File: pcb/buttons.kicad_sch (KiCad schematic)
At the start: 13 parts, among them SW1 SW_MEC_5E, SW10 SW_MEC_5E, SW11 SW_MEC_5E, SW12 SW_MEC_5E, SW13 SW_DIP_x06, SW2 SW_MEC_5E, SW3 SW_MEC_5E, SW4 SW_MEC_5E, SW5 SW_MEC_5E, SW6 SW_MEC_5E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

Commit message: Fixed ERC and DRC
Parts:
- SW1, SW10, SW11, SW12, SW2, SW3, SW4, SW5, SW6, SW7, SW8, SW9: LCSC (none) -> C318884
- SW13: LCSC (none) -> C54952
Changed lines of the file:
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@@
+      (effects (font (size 1.27 1.27)) hide)
+    )
+    (property "LCSC" "C318884" (id 4) (at 207.01 76.2 0)
       (effects (font (size 1.27 1.27)) hide)
     )
@@
       (effects (font (size 1.27 1.27)) hide)
     )
+    (property "LCSC" "C318884" (id 4) (at 181.61 95.25 0)
+      (effects (font (size 1.27 1.27)) hide)
+    )
     (pin "1")
     (pin "2")
@@
       (effects (font (size 1.27 1.27)) hide)
     )
+    (property "LCSC" "C318884" (id 4) (at 181.61 76.2 0)
+      (effects (font (size 1.27 1.27)) hide)
+    )
     (pin "1")
     (pin "2")
@@
       (effects (font (size 1.27 1.27)) hide)
     )
+    (property "LCSC" "C318884" (id 4) (at 157.48 76.2 0)
+      (effects (font (size 1.27 1.27)) hide)
+    )
     (pin "1")
     (pin "2")
@@
       (effects (font (size 1.27 1.27)) hide)
     )
+    (property "LCSC" "C318884" (id 4) (at 157.48 95.25 0)
+      (effects (font (size 1.27 1.27)) hide)
+    )
     (pin "1")
     (pin "2")
@@
       (effects (font (size 1.27 1.27)) hide)
     )
+    (property "LCSC" "C318884" (id 4) (at 134.62 95.25 0)
+      (effects (font (size 1.27 1.27)) hide)
+    )
     (pin "1")
     (pin "2")
@@
       (effects (font (size 1.27 1.27)) hide)
     )
+    (property "LCSC" "C318884" (id 4) (at 207.01 95.25 0)
+      (effects (font (size 1.27 1.27)) hide)
+    )
     (pin "1")
     (pin "2")
@@
       (effects (font (size 1.27 1.27)) hide)
     )
+    (property "LCSC" "C318884" (id 4) (at 113.03 95.25 0)
+      (effects (font (size 1.27 1.27)) hide)
+    )
     (pin "1")
     (pin "2")
@@
     )
     (property "Datasheet" "~" (id 3) (at 165.1 129.54 0)
+      (effects (font (size 1.27 1.27)) hide)
+    )
+    (property "LCSC" "C54952" (id 4) (at 165.1 129.54 0)
       (effects (font (size 1.27 1.27)) hide)
     )
@@
       (effects (font (size 1.27 1.27)) hide)
     )
+    (property "LCSC" "C318884" (id 4) (at 231.14 95.25 0)
+      (effects (font (size 1.27 1.27)) hide)
+    )
     (pin "1")
     (pin "2")
@@
       (effects (font (size 1.27 1.27)) hide)
     )
+    (property "LCSC" "C318884" (id 4) (at 134.62 76.2 0)
+      (effects (font (size 1.27 1.27)) hide)
+    )
     (pin "1")
     (pin "2")
@@
       (effects (font (size 1.27 1.27)) hide)
     )
+    (property "LCSC" "C318884" (id 4) (at 231.14 76.2 0)
+      (effects (font (size 1.27 1.27)) hide)
+    )
     (pin "1")
     (pin "2")
@@
       (effects (font (size 1.27 1.27)) hide)
     )
+    (property "LCSC" "C318884" (id 4) (at 113.03 76.2 0)
+      (effects (font (size 1.27 1.27)) hide)
+    )

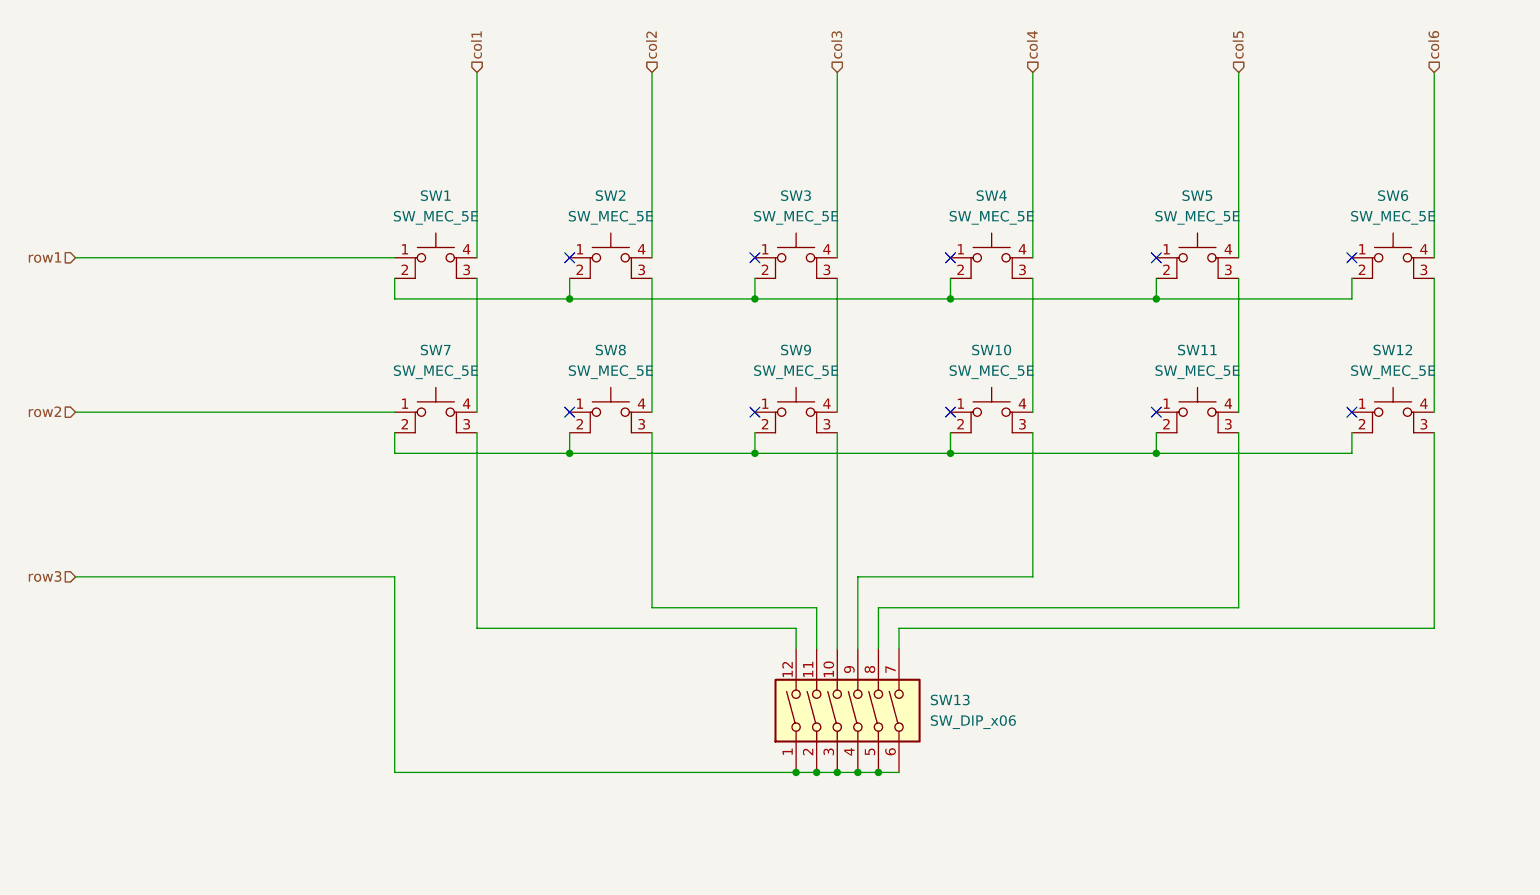
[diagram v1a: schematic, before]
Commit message: Added diodes to key matrix
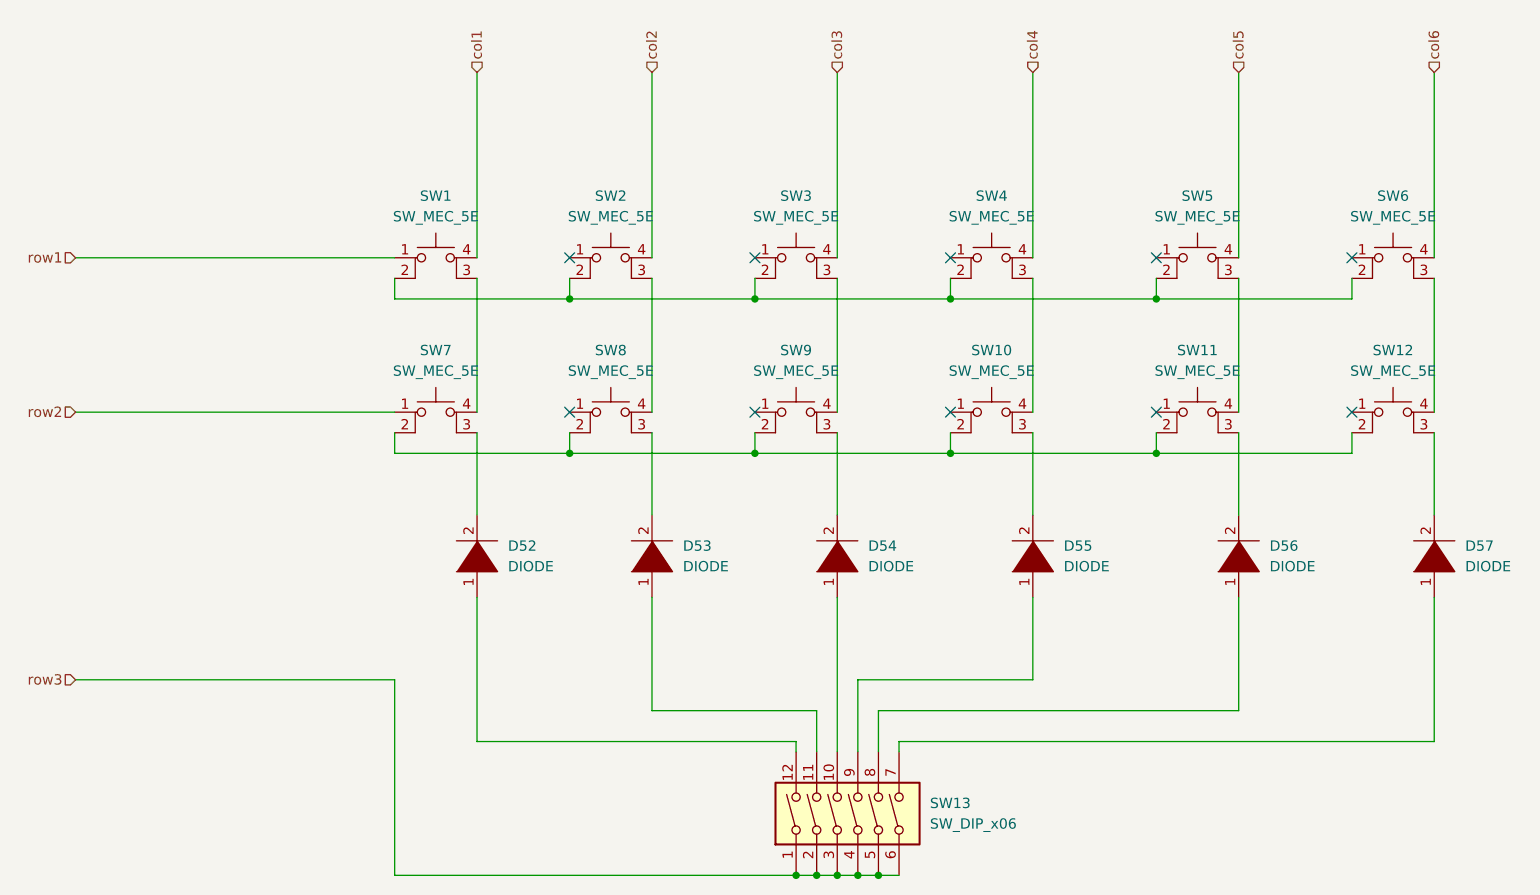
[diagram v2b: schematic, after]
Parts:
- added D52, D53, D54, D55, D56, D57: DIODE, Diode_SMD:D_SOD-123F, symbol pspice:DIODE
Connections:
- net at SW10.3 (K): now also D55.2 (A); no longer SW13.9
- net at SW9.3 (K): now also D54.2 (A); no longer SW13.10
- net at SW8.3 (K): now also D53.2 (A); no longer SW13.11
- net at SW11.3 (K): now also D56.2 (A); no longer SW13.8
- net at SW7.3 (K): now also D52.2 (A); no longer SW13.12
- net at SW13.7: now also D57.1 (K); no longer SW12.3 (K)
- new net: D57.2 (A), SW12.3 (K)
- new net: D56.1 (K), SW13.8
- new net: D54.1 (K), SW13.10
- new net: D53.1 (K), SW13.11
- new net: D52.1 (K), SW13.12
- new net: D55.1 (K), SW13.9
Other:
- moved on the sheet: SW13

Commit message: Small fixed for new board
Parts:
- D52, D53, D54, D55, D56, D57: symbol pspice:DIODE -> Diode:SM4007
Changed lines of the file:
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@@
-    (stroke (width 0) (type default) (color 0 0 0 0))
-  )
-  (wire (pts (xy 118.11 95.25) (xy 118.11 105.41))
     (stroke (width 0) (type default) (color 0 0 0 0))
   )
@@
     (stroke (width 0) (type default) (color 0 0 0 0))
   )
-  (wire (pts (xy 162.56 115.57) (xy 162.56 134.62))
+  (wire (pts (xy 162.56 114.3) (xy 162.56 134.62))
     (stroke (width 0) (type default) (color 0 0 0 0))
   )
@@
     (stroke (width 0) (type default) (color 0 0 0 0))
   )
-  (wire (pts (xy 186.69 95.25) (xy 186.69 105.41))
+  (wire (pts (xy 186.69 95.25) (xy 186.69 106.68))
     (stroke (width 0) (type default) (color 0 0 0 0))
   )
@@
     (stroke (width 0) (type default) (color 0 0 0 0))
   )
+  (wire (pts (xy 212.09 114.3) (xy 212.09 129.54))
+    (stroke (width 0) (type default) (color 0 0 0 0))
+  )
   (wire (pts (xy 139.7 76.2) (xy 139.7 92.71))
     (stroke (width 0) (type default) (color 0 0 0 0))
@@
     (stroke (width 0) (type default) (color 0 0 0 0))
   )
+  (wire (pts (xy 118.11 114.3) (xy 118.11 133.35))
+    (stroke (width 0) (type default) (color 0 0 0 0))
+  )
   (wire (pts (xy 167.64 134.62) (xy 167.64 129.54))
     (stroke (width 0) (type default) (color 0 0 0 0))
@@
     (stroke (width 0) (type default) (color 0 0 0 0))
   )
+  (wire (pts (xy 118.11 95.25) (xy 118.11 106.68))
+    (stroke (width 0) (type default) (color 0 0 0 0))
+  )
   (wire (pts (xy 201.93 95.25) (xy 201.93 97.79))
     (stroke (width 0) (type default) (color 0 0 0 0))
   )
-  (wire (pts (xy 212.09 95.25) (xy 212.09 105.41))
-    (stroke (width 0) (type default) (color 0 0 0 0))
-  )
-  (wire (pts (xy 139.7 115.57) (xy 139.7 129.54))
+  (wire (pts (xy 212.09 95.25) (xy 212.09 106.68))
     (stroke (width 0) (type default) (color 0 0 0 0))
   )
@@
     (stroke (width 0) (type default) (color 0 0 0 0))
   )
-  (wire (pts (xy 236.22 95.25) (xy 236.22 105.41))
+  (wire (pts (xy 236.22 95.25) (xy 236.22 106.68))
     (stroke (width 0) (type default) (color 0 0 0 0))
   )
@@
     (stroke (width 0) (type default) (color 0 0 0 0))
   )
-  (wire (pts (xy 162.56 95.25) (xy 162.56 105.41))
+  (wire (pts (xy 162.56 95.25) (xy 162.56 106.68))
     (stroke (width 0) (type default) (color 0 0 0 0))
   )
@@
     (stroke (width 0) (type default) (color 0 0 0 0))
   )
-  (wire (pts (xy 186.69 115.57) (xy 186.69 125.73))
+  (wire (pts (xy 186.69 114.3) (xy 186.69 125.73))
     (stroke (width 0) (type default) (color 0 0 0 0))
   )
@@
     (stroke (width 0) (type default) (color 0 0 0 0))
   )
+  (wire (pts (xy 139.7 114.3) (xy 139.7 129.54))
+    (stroke (width 0) (type default) (color 0 0 0 0))
+  )
   (wire (pts (xy 201.93 97.79) (xy 226.06 97.79))
     (stroke (width 0) (type default) (color 0 0 0 0))
@@
     (stroke (width 0) (type default) (color 0 0 0 0))
   )
-  (wire (pts (xy 236.22 115.57) (xy 236.22 133.35))
+  (wire (pts (xy 236.22 114.3) (xy 236.22 133.35))
     (stroke (width 0) (type default) (color 0 0 0 0))
   )
@@
     (stroke (width 0) (type default) (color 0 0 0 0))
   )
-  (wire (pts (xy 212.09 115.57) (xy 212.09 129.54))
-    (stroke (width 0) (type default) (color 0 0 0 0))
-  )
   (wire (pts (xy 167.64 129.54) (xy 212.09 129.54))
     (stroke (width 0) (type default) (color 0 0 0 0))
@@
     (stroke (width 0) (type default) (color 0 0 0 0))
   )
-  (wire (pts (xy 118.11 115.57) (xy 118.11 133.35))
-    (stroke (width 0) (type default) (color 0 0 0 0))
-  )
-  (wire (pts (xy 139.7 95.25) (xy 139.7 105.41))
+  (wire (pts (xy 139.7 95.25) (xy 139.7 106.68))
     (stroke (width 0) (type default) (color 0 0 0 0))
   )
@@
     (pin "4")
   )
-  (symbol (lib_id "pspice:DIODE") (at 236.22 110.49 90) (unit 1)
+  (symbol (lib_id "Diode:SM4007") (at 236.22 110.49 90) (unit 1)
     (in_bom yes) (on_board yes) (fields_autoplaced)
     (property "Reference" "D57" (id 0) (at 240.03 109.2199 90)
@@
       (effects (font (size 1.27 1.27)) (justify right))
     )
-    (property "Footprint" "Diode_SMD:D_SOD-123F" (id 2) (at 236.22 110.49 0)
-      (effects (font (size 1.27 1.27)) hide)
-    )
-    (property "Datasheet" "~" (id 3) (at 236.22 110.49 0)
+    (property "Footprint" "Diode_SMD:D_SOD-123F" (id 2) (at 240.665 110.49 0)
+      (effects (font (size 1.27 1.27)) hide)
+    )
+    (property "Datasheet" "http://cdn-reichelt.de/documents/datenblatt/A400/SMD1N400%23DIO.pdf" (id 3) (at 236.22 110.49 0)
       (effects (font (size 1.27 1.27)) hide)
     )
@@
     (pin "4")
   )
-  (symbol (lib_id "pspice:DIODE") (at 212.09 110.49 90) (unit 1)
+  (symbol (lib_id "Diode:SM4007") (at 212.09 110.49 90) (unit 1)
     (in_bom yes) (on_board yes) (fields_autoplaced)
     (property "Reference" "D56" (id 0) (at 215.9 109.2199 90)
@@
       (effects (font (size 1.27 1.27)) (justify right))
     )
-    (property "Footprint" "Diode_SMD:D_SOD-123F" (id 2) (at 212.09 110.49 0)
-      (effects (font (size 1.27 1.27)) hide)
-    )
-    (property "Datasheet" "~" (id 3) (at 212.09 110.49 0)
+    (property "Footprint" "Diode_SMD:D_SOD-123F" (id 2) (at 216.535 110.49 0)
+      (effects (font (size 1.27 1.27)) hide)
+    )
+    (property "Datasheet" "http://cdn-reichelt.de/documents/datenblatt/A400/SMD1N400%23DIO.pdf" (id 3) (at 212.09 110.49 0)
       (effects (font (size 1.27 1.27)) hide)
     )
@@
     (pin "2")
   )
-  (symbol (lib_id "pspice:DIODE") (at 162.56 110.49 90) (unit 1)
+  (symbol (lib_id "Diode:SM4007") (at 162.56 110.49 90) (unit 1)
     (in_bom yes) (on_board yes) (fields_autoplaced)
     (property "Reference" "D54" (id 0) (at 166.37 109.2199 90)
@@
       (effects (font (size 1.27 1.27)) (justify right))
     )
-    (property "Footprint" "Diode_SMD:D_SOD-123F" (id 2) (at 162.56 110.49 0)
-      (effects (font (size 1.27 1.27)) hide)
-    )
-    (property "Datasheet" "~" (id 3) (at 162.56 110.49 0)
+    (property "Footprint" "Diode_SMD:D_SOD-123F" (id 2) (at 167.005 110.49 0)
+      (effects (font (size 1.27 1.27)) hide)
+    )
+    (property "Datasheet" "http://cdn-reichelt.de/documents/datenblatt/A400/SMD1N400%23DIO.pdf" (id 3) (at 162.56 110.49 0)
       (effects (font (size 1.27 1.27)) hide)
     )
@@
     (pin "4")
   )
-  (symbol (lib_id "pspice:DIODE") (at 118.11 110.49 90) (unit 1)
+  (symbol (lib_id "Diode:SM4007") (at 118.11 110.49 90) (unit 1)
     (in_bom yes) (on_board yes) (fields_autoplaced)
     (property "Reference" "D52" (id 0) (at 121.92 109.2199 90)
@@
       (effects (font (size 1.27 1.27)) (justify right))
     )
-    (property "Footprint" "Diode_SMD:D_SOD-123F" (id 2) (at 118.11 110.49 0)
-      (effects (font (size 1.27 1.27)) hide)
-    )
-    (property "Datasheet" "~" (id 3) (at 118.11 110.49 0)
+    (property "Footprint" "Diode_SMD:D_SOD-123F" (id 2) (at 122.555 110.49 0)
+      (effects (font (size 1.27 1.27)) hide)
+    )
+    (property "Datasheet" "http://cdn-reichelt.de/documents/datenblatt/A400/SMD1N400%23DIO.pdf" (id 3) (at 118.11 110.49 0)
       (effects (font (size 1.27 1.27)) hide)
     )
@@
     (pin "4")
   )
-  (symbol (lib_id "pspice:DIODE") (at 186.69 110.49 90) (unit 1)
+  (symbol (lib_id "Diode:SM4007") (at 186.69 110.49 90) (unit 1)
     (in_bom yes) (on_board yes) (fields_autoplaced)
     (property "Reference" "D55" (id 0) (at 190.5 109.2199 90)
@@
       (effects (font (size 1.27 1.27)) (justify right))
     )
-    (property "Footprint" "Diode_SMD:D_SOD-123F" (id 2) (at 186.69 110.49 0)
-      (effects (font (size 1.27 1.27)) hide)
-    )
-    (property "Datasheet" "~" (id 3) (at 186.69 110.49 0)
+    (property "Footprint" "Diode_SMD:D_SOD-123F" (id 2) (at 191.135 110.49 0)
+      (effects (font (size 1.27 1.27)) hide)
+    )
+    (property "Datasheet" "http://cdn-reichelt.de/documents/datenblatt/A400/SMD1N400%23DIO.pdf" (id 3) (at 186.69 110.49 0)
       (effects (font (size 1.27 1.27)) hide)
     )
@@
     (pin "4")
   )
-  (symbol (lib_id "pspice:DIODE") (at 139.7 110.49 90) (unit 1)
+  (symbol (lib_id "Diode:SM4007") (at 139.7 110.49 90) (unit 1)
     (in_bom yes) (on_board yes) (fields_autoplaced)
     (property "Reference" "D53" (id 0) (at 143.51 109.2199 90)
@@
       (effects (font (size 1.27 1.27)) (justify right))
     )
-    (property "Footprint" "Diode_SMD:D_SOD-123F" (id 2) (at 139.7 110.49 0)
-      (effects (font (size 1.27 1.27)) hide)
-    )
-    (property "Datasheet" "~" (id 3) (at 139.7 110.49 0)
-      (effects (font (size 1.27 1.27)) hide)
-    )
+    (property "Footprint" "Diode_SMD:D_SOD-123F" (id 2) (at 144.145 110.49 0)
+      (effects (font (size 1.27 1.27)) hide)
+    )
+    (property "Datasheet" "http://cdn-reichelt.de/documents/datenblatt/A400/SMD1N400%23DIO.pdf" (id 3) (at 139.7 110.49 0)
+      (effects (font (size 1.27 1.27)) hide)
+    )
